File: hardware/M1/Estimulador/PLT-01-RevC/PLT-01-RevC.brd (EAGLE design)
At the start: 94 x 66 mm, 56 parts, among them T1 2N2222, T2 2N2222, T3 2N2222, T4 2N2222, T5 2N2222, T6 2N2222

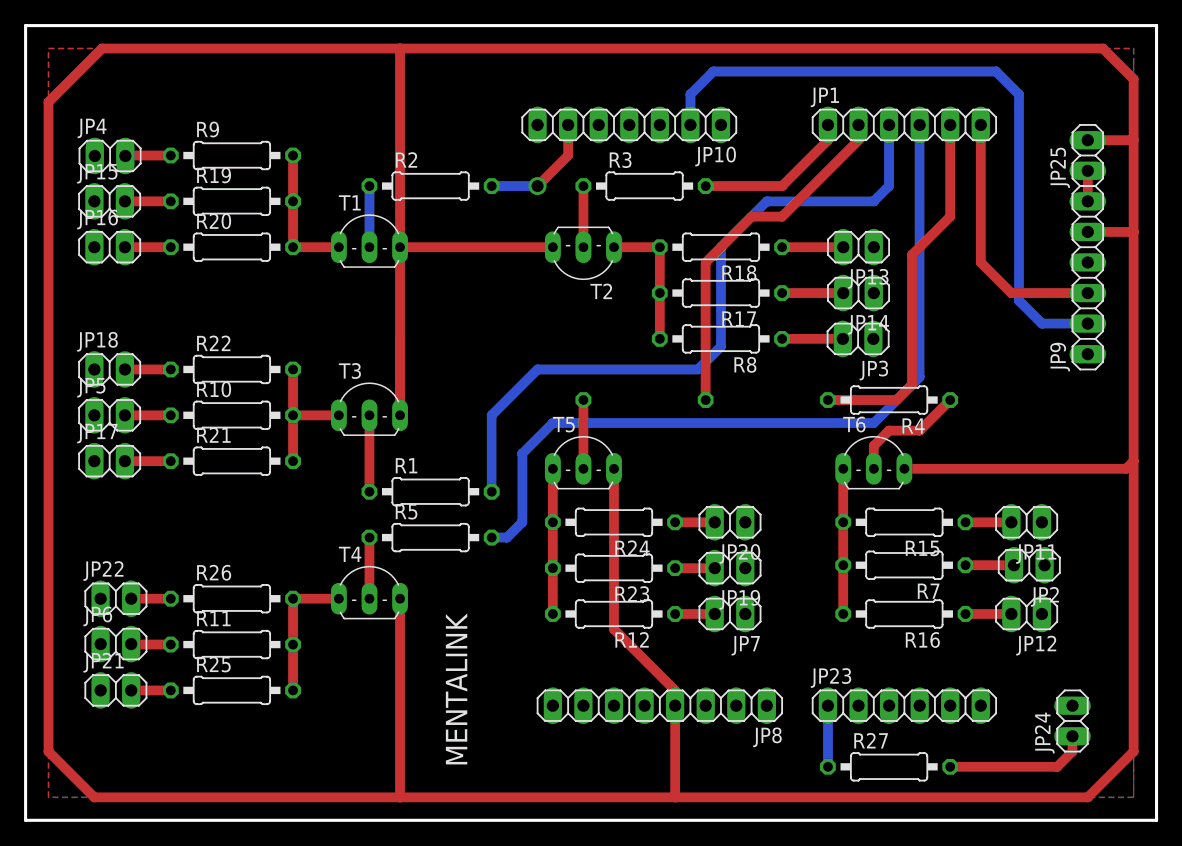
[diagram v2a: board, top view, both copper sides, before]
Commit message: Se agregan agujeros a placa M1
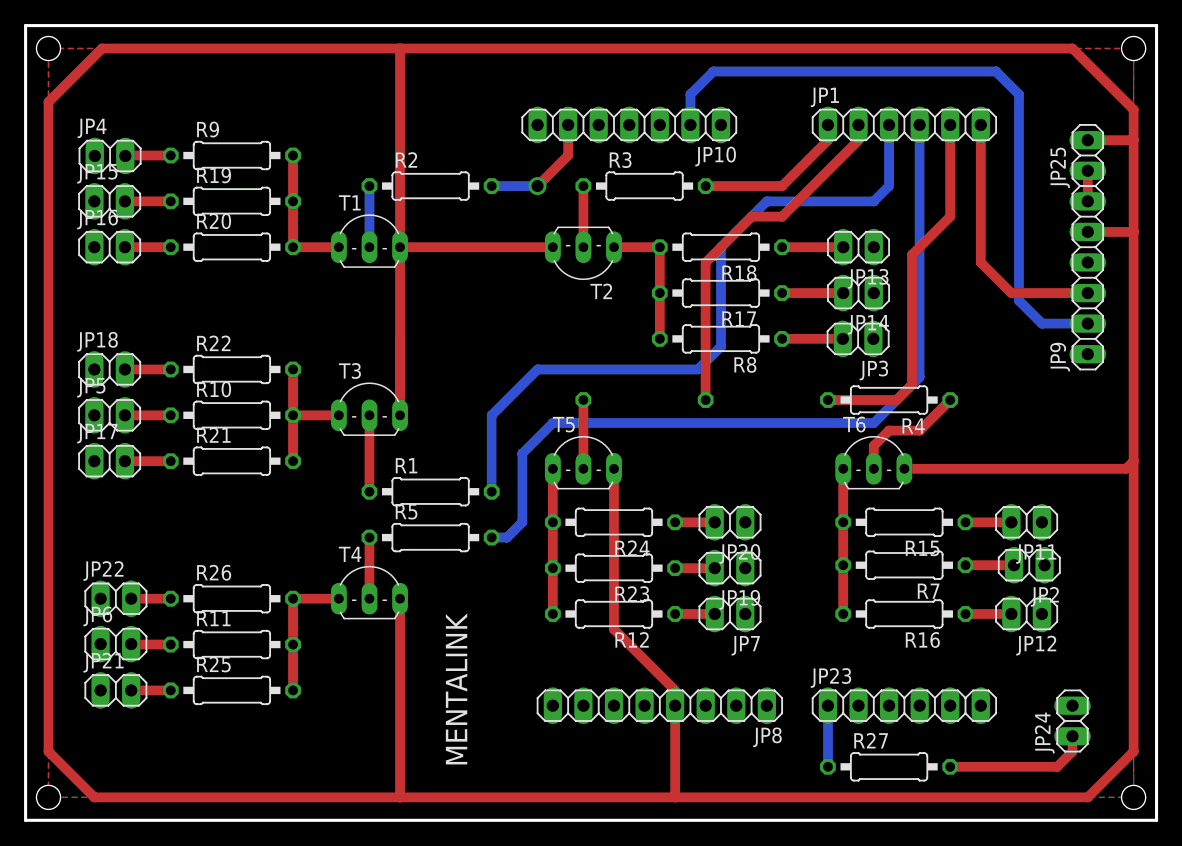
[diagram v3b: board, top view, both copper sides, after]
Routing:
- net 5V: track 418.6 -> 417.1 mm
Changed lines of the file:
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@@
 <layer number="43" name="vRestrict" color="2" fill="10" visible="yes" active="yes"/>
 <layer number="44" name="Drills" color="7" fill="1" visible="no" active="yes"/>
-<layer number="45" name="Holes" color="7" fill="1" visible="no" active="yes"/>
+<layer number="45" name="Holes" color="7" fill="1" visible="yes" active="yes"/>
 <layer number="46" name="Milling" color="3" fill="1" visible="no" active="yes"/>
 <layer number="47" name="Measures" color="7" fill="1" visible="no" active="yes"/>
@@
 <wire x1="93.345" y1="-0.635" x2="-0.635" y2="-0.635" width="0.254" layer="20"/>
 <wire x1="-0.635" y1="-0.635" x2="-0.635" y2="65.405" width="0.254" layer="20"/>
+<hole x="1.27" y="63.5" drill="2"/>
+<hole x="91.44" y="63.5" drill="2"/>
+<hole x="91.44" y="1.27" drill="2"/>
+<hole x="1.27" y="1.27" drill="2"/>
 </plain>
 <attributes>
@@
 <wire x1="91.44" y1="29.21" x2="91.44" y2="48.26" width="0.8128" layer="1"/>
 <wire x1="91.44" y1="48.26" x2="91.44" y2="55.88" width="0.8128" layer="1"/>
-<wire x1="91.44" y1="55.88" x2="91.44" y2="60.96" width="0.8128" layer="1"/>
-<wire x1="91.44" y1="60.96" x2="88.9" y2="63.5" width="0.8128" layer="1"/>
-<wire x1="88.9" y1="63.5" x2="30.48" y2="63.5" width="0.8128" layer="1"/>
+<wire x1="91.44" y1="55.88" x2="91.44" y2="58.42" width="0.8128" layer="1"/>
+<wire x1="86.36" y1="63.5" x2="30.48" y2="63.5" width="0.8128" layer="1"/>
 <wire x1="72.39" y1="28.575" x2="90.805" y2="28.575" width="0.8128" layer="1"/>
 <wire x1="90.805" y1="28.575" x2="91.44" y2="29.21" width="0.8128" layer="1"/>
@@
 <contactref element="JP25" pad="2"/>
 <wire x1="87.63" y1="55.88" x2="91.44" y2="55.88" width="0.8128" layer="1"/>
+<wire x1="91.44" y1="58.42" x2="86.36" y2="63.5" width="0.8128" layer="1"/>
 </signal>
 <signal name="N$11">
